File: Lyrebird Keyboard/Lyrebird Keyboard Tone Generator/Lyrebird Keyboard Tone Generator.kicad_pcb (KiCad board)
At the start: 2 copper layers, 8.4 x 51.3 mm, 269 parts, among them IC1 LM358DT, IC10 LM358DT, IC11 LM358DT, IC12 LM358DT, IC13 HEF4069UBT,653, IC14 HEF4069UBT,653, IC15 MC14024BDG, IC16 MC14024BDG, IC17 MC14024BDG, IC18 MC14024BDG, IC19 MC14024BDG, IC2 LM358DT, IC20 MC14024BDG, IC21 MC14024BDG, IC22 MC14024BDG, IC23 MC14024BDG, IC24 MC14024BDG, IC25 MC14024BDG, IC26 MC14024BDG, IC3 LM358DT, IC4 LM358DT, IC5 LM358DT, IC6 LM358DT, IC7 LM358DT, IC8 LM358DT, IC9 LM358DT, J1 Edge Connector, J10 C# 4434 Hz, J11 G# 6642 Hz, J12 D 4697 Hz, J13 F# 5923 Hz, J2 A 3520 Hz, J3 D# 4976 Hz, J4 A# 3726 Hz, J5 E 5274 Hz, J6 B 3949 Hz, J7 F 5590 Hz, J8 C 4188 Hz, J9 G 6275 Hz

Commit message: Further Tone Generator Work, Diode mixers placed
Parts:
- C1, C10, C11, C12, C7, C8, C9, IC1, IC10, IC11, IC12, IC7, IC8, IC9, J11, J13, J2, J3, J5, J7, J9, R1, R2, R25, R26, R27, R28, R29, R3, R30, R31, R32, R33, R34, R35, R36, R37, R38, R39, R4, R40, R41, R42, R43, R44, R45, R46, R47, R48, Z1, Z13, Z14, Z15, Z16, Z17, Z18, Z19, Z2, Z20, Z21, Z22, Z23, Z24: moved to F.Cu
- D1, D10, D100, D101, D102, D103, D104, D105, D106, D107, D108, D109, D11, D110, D111, D112, D113, D114, D115, D116, D117, D118, D119, D12, D120, D121, D122, D123, D124, D125, D126, D127, D128, D129, D130, D131, D132, D133, D134, D135, D136, D137, D138, D139, D14, D140, D141, D142, D143, D144, D145, D146, D15, D16, D17, D18, D19, D2, D20, D21, D22, D23, D24, D25, D26, D27, D28, D29, D3, D30, D31, D32, D33, D34, D35, D36, D37, D38, D39, D4, D40, D41, D42, D43, D44, D45, D46, D47, D48, D49, D5, D50, D51, D52, D53, D54, D55, D56, D57, D58, D59, D6, D60, D61, D62, D63, D64, D65, D66, D67, D68, D69, D7, D70, D71, D72, D73, D74, D75, D76, D77, D78, D79, D8, D80, D81, D82, D83, D84, D85, D86, D87, D88, D89, D9, D90, D91, D92, D93, D94, D95, D96, D97, D98, D99: value 1N4148W -> 1N4148; footprint Diode_SMD:D_SOD-123 -> Diode_THT:D_DO-35_SOD27_P7.62mm_Horizontal
- IC15, IC16, IC17, IC18, IC19, IC20, IC21, IC22, IC23, IC24, IC25, IC26: value MC14024BDG -> CD4024BE; footprint SamacSys_Parts:SOIC127P600X175-14N -> SamacSys_Parts:DIP794W53P254L1930H508Q14N
- moved IC13 244.6 mm to (256.8, 83.6)
- moved IC14 216.1 mm to (237.2, 95.8)
- moved C1 144.7 mm to (216.0, 153.3), turned to 0 degrees
- moved IC1 144.7 mm to (216.0, 153.3), turned to 0 degrees
- moved J2 144.7 mm to (216.0, 153.3), turned to 0 degrees
- moved R1 144.7 mm to (216.0, 153.3), turned to 0 degrees
- moved R2 144.7 mm to (216.0, 153.3), turned to 0 degrees
- moved R3 144.7 mm to (216.0, 153.3), turned to 0 degrees
- moved R4 144.7 mm to (216.0, 153.3), turned to 0 degrees
- moved Z1 144.7 mm to (216.0, 153.3), turned to 0 degrees
- moved Z2 144.7 mm to (216.0, 153.3), turned to 0 degrees
- moved J9 131.7 mm to (215.3, 65.7)
- moved Z22 131.4 mm to (220.4, 71.5), turned to 0 degrees
- moved Z16 128.0 mm to (215.8, 71.5), turned to 0 degrees
- moved J4 126.3 mm to (186.9, 65.8), turned to 180 degrees
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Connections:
- D10 pad 1: Q5 -> Q5A
- D100 pad 1: Q2 -> Q3F#
- D100 pad 2: F#50S -> F#38S
- D101 pad 1: Q2 -> Q3G
- D101 pad 2: G51S -> G39S
- D102 pad 1: Q2 -> Q3G#
- D102 pad 2: G#52S -> G#40S
- D103 pad 1: Q3 -> Q3D#
- D104 pad 1: Q3 -> Q3E
- D105 pad 1: Q3 -> Q3F
- D106 pad 1: Q3 -> Q4F#
- D106 pad 2: F#50S -> F#38S
- D107 pad 1: Q3 -> Q4G
- D107 pad 2: G51S -> G39S
- D108 pad 1: Q3 -> Q4G#
- D108 pad 2: G#52S -> G#40S
- D109 pad 1: Q3 -> Q3D#
- D11 pad 1: Q5 -> Q5A
- D110 pad 1: Q3 -> Q3E
- D111 pad 1: Q3 -> Q3F
- D112 pad 1: Q3 -> Q4F#
- D112 pad 2: F#38S -> F#26S
- D113 pad 1: Q3 -> Q4G
- D113 pad 2: G39S -> G27S
- D114 pad 1: Q3 -> Q4G#
- D114 pad 2: G#40S -> G#28S
- D115 pad 1: Q4 -> Q4D#
- D116 pad 1: Q4 -> Q4E
- D117 pad 1: Q4 -> Q4F
- D118 pad 1: Q4 -> Q5F#
- D118 pad 2: F#38S -> F#26S
- D119 pad 1: Q4 -> Q5G
- D119 pad 2: G39S -> G27S
- D12 pad 1: Q6 -> Q6A
- D120 pad 1: Q4 -> Q5G#
- D120 pad 2: G#40S -> G#28S
- D121 pad 1: Q4 -> Q4D#
- D122 pad 1: Q4 -> Q4E
- D123 pad 1: Q4 -> Q4F
- D124 pad 1: Q4 -> Q5F#
- D124 pad 2: F#26S -> F#14S
- D125 pad 1: Q4 -> Q5G
- D125 pad 2: G27S -> G15S
- D126 pad 1: Q4 -> Q5G#
- D126 pad 2: G#28S -> G#16S
- D127 pad 1: Q5 -> Q5D#
- D128 pad 1: Q5 -> Q5E
- D129 pad 1: Q5 -> Q5F
- D130 pad 1: Q5 -> Q6F#
- D130 pad 2: F#26S -> F#14S
- D131 pad 1: Q5 -> Q6G
- D131 pad 2: G27S -> G15S
- D132 pad 1: Q5 -> Q6G#
- D132 pad 2: G#28S -> G#16S
- D133 pad 1: Q5 -> Q5D#
- D134 pad 1: Q5 -> Q5E
- D135 pad 1: Q5 -> Q5F
- D136 pad 1: Q5 -> Q6F#
- D136 pad 2: F#14S -> F#2S
- D137 pad 1: Q5 -> Q6G
- D137 pad 2: G15S -> G3S
- D138 pad 1: Q5 -> Q6G#
- D138 pad 2: G#16S -> G#4S
- D139 pad 1: Q6 -> Q6D#
- D14 pad 1: Q1 -> Q1A#
- D140 pad 1: Q6 -> Q6E
- D141 pad 1: Q6 -> Q6F
- D142 pad 1: Q6 -> Q7F#
- D142 pad 2: F#14S -> F#2S
- D143 pad 1: Q6 -> Q7G
- D143 pad 2: G15S -> G3S
- D144 pad 1: Q6 -> Q7G#
- D144 pad 2: G#16S -> G#4S
- D145 pad 1: Q6 -> Q6F
- D146 pad 1: Q7 -> Q7F
- D15 pad 1: Q1 -> Q1A#
- D16 pad 1: Q2 -> Q2A#
- D17 pad 1: Q2 -> Q2A#
- D18 pad 1: Q3 -> Q3A#
- D19 pad 1: Q3 -> Q3A#
- D2 pad 1: Q1 -> Q1A
- D20 pad 1: Q4 -> Q4A#
- D21 pad 1: Q4 -> Q4A#
- D22 pad 1: Q5 -> Q5A#
- D23 pad 1: Q5 -> Q5A#
- D24 pad 1: Q6 -> Q6A#
- D26 pad 1: Q1 -> Q1B
- D27 pad 1: Q1 -> Q1B
- D28 pad 1: Q2 -> Q2B
- D29 pad 1: Q2 -> Q2B
- D3 pad 1: Q1 -> Q1A
- D30 pad 1: Q3 -> Q3B
- D31 pad 1: Q3 -> Q3B
- D32 pad 1: Q4 -> Q4B
- D33 pad 1: Q4 -> Q4B
- D34 pad 1: Q5 -> Q5B
- D35 pad 1: Q5 -> Q5B
- D36 pad 1: Q6 -> Q6B
- D38 pad 1: Q1 -> Q1C
- D39 pad 1: Q1 -> Q1C
- D4 pad 1: Q2 -> Q2A
- D40 pad 1: Q2 -> Q2C
- D41 pad 1: Q2 -> Q2C
- D42 pad 1: Q3 -> Q3C
- D43 pad 1: Q3 -> Q3C
- D44 pad 1: Q4 -> Q4C
- D45 pad 1: Q4 -> Q4C
- D46 pad 1: Q5 -> Q5C
- D47 pad 1: Q5 -> Q5C
- D48 pad 1: Q6 -> Q6C
- D5 pad 1: Q2 -> Q2A
- D50 pad 1: Q1 -> Q1C#
- D51 pad 1: Q1 -> Q1C#
- D52 pad 1: Q2 -> Q2C#
- D53 pad 1: Q2 -> Q2C#
- D54 pad 1: Q3 -> Q3C#
- D55 pad 1: Q3 -> Q3C#
- D56 pad 1: Q4 -> Q4C#
- D57 pad 1: Q4 -> Q4C#
- D58 pad 1: Q5 -> Q5C#
- D59 pad 1: Q5 -> Q5C#
- D6 pad 1: Q3 -> Q3A
- D60 pad 1: Q6 -> Q6C#
- D62 pad 1: Q1 -> Q1D
- D63 pad 1: Q1 -> Q1D
- D64 pad 1: Q2 -> Q2D
- D65 pad 1: Q2 -> Q2D
- D66 pad 1: Q3 -> Q3D
- D67 pad 1: Q3 -> Q3D
- D68 pad 1: Q4 -> Q4D
- D69 pad 1: Q4 -> Q4D
- D7 pad 1: Q3 -> Q3A
- D70 pad 1: Q5 -> Q5D
- D71 pad 1: Q5 -> Q5D
- D72 pad 1: Q6 -> Q6D
- D76 pad 1: Q6 -> Q1F#
- D76 pad 2: F#2S -> F#62S
- D77 pad 1: Q6 -> Q1G
- D77 pad 2: G3S -> G63S
- D78 pad 1: Q7 -> Q2G
- D78 pad 2: G3S -> G63S
- D79 pad 1: Q1 -> Q1D#
- D8 pad 1: Q4 -> Q4A
- D80 pad 1: Q1 -> Q1E
- D81 pad 1: Q1 -> Q1F
- D82 pad 1: Q7 -> Q2F#
- D82 pad 2: F#2S -> F#62S
- D83 pad 1: Q6 -> Q1G#
- D83 pad 2: G#4S -> G#64S
- D84 pad 1: Q7 -> Q2G#
- D84 pad 2: G#4S -> G#64S
- D85 pad 1: Q1 -> Q1D#
- D86 pad 1: Q1 -> Q1E
- D87 pad 1: Q1 -> Q1F
- D88 pad 1: Q1 -> Q2F#
- D88 pad 2: F#62S -> F#50S
- D89 pad 1: Q1 -> Q2G
- D89 pad 2: G63S -> G51S
- D9 pad 1: Q4 -> Q4A
- D90 pad 1: Q1 -> Q2G#
- D90 pad 2: G#64S -> G#52S
- D91 pad 1: Q2 -> Q2D#
- D92 pad 1: Q2 -> Q2E
- D93 pad 1: Q2 -> Q2F
- D94 pad 1: Q2 -> Q3F#
- D94 pad 2: F#62S -> F#50S
- D95 pad 1: Q2 -> Q3G
- D95 pad 2: G63S -> G51S
- D96 pad 1: Q2 -> Q3G#
- D96 pad 2: G#64S -> G#52S
- D97 pad 1: Q2 -> Q2D#
- D98 pad 1: Q2 -> Q2E
- D99 pad 1: Q2 -> Q2F
- IC15 pad 11: Q2 -> Q2A
- IC15 pad 12: Q1 -> Q1A
- IC15 pad 4: Q6 -> Q6A
- IC15 pad 5: Q5 -> Q5A
- IC15 pad 6: Q4 -> Q4A
- IC15 pad 9: Q3 -> Q3A
- IC16 pad 11: Q2 -> Q2A#
- IC16 pad 12: Q1 -> Q1A#
- IC16 pad 4: Q6 -> Q6A#
- IC16 pad 5: Q5 -> Q5A#
- IC16 pad 6: Q4 -> Q4A#
- IC16 pad 9: Q3 -> Q3A#
- IC17 pad 11: Q2 -> Q2B
- IC17 pad 12: Q1 -> Q1B
- IC17 pad 4: Q6 -> Q6B
- IC17 pad 5: Q5 -> Q5B
- IC17 pad 6: Q4 -> Q4B
- IC17 pad 9: Q3 -> Q3B
- IC18 pad 11: Q2 -> Q2C
- IC18 pad 12: Q1 -> Q1C
- IC18 pad 4: Q6 -> Q6C
- IC18 pad 5: Q5 -> Q5C
- IC18 pad 6: Q4 -> Q4C
- IC18 pad 9: Q3 -> Q3C
- IC19 pad 11: Q2 -> Q2C#
- IC19 pad 12: Q1 -> Q1C#
- IC19 pad 4: Q6 -> Q6C#
- IC19 pad 5: Q5 -> Q5C#
- IC19 pad 6: Q4 -> Q4C#
- IC19 pad 9: Q3 -> Q3C#
- IC20 pad 11: Q2 -> Q2D
- IC20 pad 12: Q1 -> Q1D
- IC20 pad 4: Q6 -> Q6D
- IC20 pad 5: Q5 -> Q5D
- IC20 pad 6: Q4 -> Q4D
- IC20 pad 9: Q3 -> Q3D
- IC21 pad 11: Q2 -> Q2D#
- IC21 pad 12: Q1 -> Q1D#
- IC21 pad 4: Q6 -> Q6D#
- IC21 pad 5: Q5 -> Q5D#
- IC21 pad 6: Q4 -> Q4D#
- IC21 pad 9: Q3 -> Q3D#
- IC22 pad 11: Q2 -> Q2E
- IC22 pad 12: Q1 -> Q1E
- IC22 pad 4: Q6 -> Q6E
- IC22 pad 5: Q5 -> Q5E
- IC22 pad 6: Q4 -> Q4E
- IC22 pad 9: Q3 -> Q3E
- IC23 pad 11: Q2 -> Q2F
- IC23 pad 12: Q1 -> Q1F
- IC23 pad 3: Q7 -> Q7F
- IC23 pad 4: Q6 -> Q6F
- IC23 pad 5: Q5 -> Q5F
- IC23 pad 6: Q4 -> Q4F
- IC23 pad 9: Q3 -> Q3F
- IC24 pad 11: Q2 -> Q2F#
- IC24 pad 12: Q1 -> Q1F#
- IC24 pad 3: unconnected-(IC24-Q7-Pad3) -> Q7F#
- IC24 pad 4: Q6 -> Q6F#
- IC24 pad 5: Q5 -> Q5F#
- IC24 pad 6: Q4 -> Q4F#
- IC24 pad 9: Q3 -> Q3F#
- IC25 pad 11: Q2 -> Q2G
- IC25 pad 12: Q1 -> Q1G
- IC25 pad 3: Q7 -> Q7G
- IC25 pad 4: Q6 -> Q6G
- IC25 pad 5: Q5 -> Q5G
- IC25 pad 6: Q4 -> Q4G
- IC25 pad 9: Q3 -> Q3G
- IC26 pad 11: Q2 -> Q2G#
- IC26 pad 12: Q1 -> Q1G#
- IC26 pad 3: Q7 -> Q7G#
- IC26 pad 4: Q6 -> Q6G#
- IC26 pad 5: Q5 -> Q5G#
- IC26 pad 6: Q4 -> Q4G#
- IC26 pad 9: Q3 -> Q3G#
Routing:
- net +15V: track 0.00 -> 405.4 mm
- net -15V: track 0.00 -> 183.7 mm
- net E36S: track 0.00 -> 157.0 mm
- net G39S: track 0.00 -> 153.7 mm
- net D#35S: track 0.00 -> 150.3 mm
- net F37S: track 0.00 -> 149.0 mm
- net F#38S: track 0.00 -> 140.2 mm
- net D#23S: track 0.00 -> 138.4 mm
- net F25S: track 0.00 -> 138.4 mm
- net E24S: track 0.00 -> 135.6 mm
- net D#11S: track 0.00 -> 133.5 mm
- net F13S: track 0.00 -> 132.8 mm
- net E12S: track 0.00 -> 130.6 mm
- net F1S: track 0.00 -> 127.7 mm
- net D#47S: track 0.00 -> 127.3 mm
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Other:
- board size 8.4 x 51.3 mm -> 186.8 x 75.5 mm
- copper layers 2 -> 4

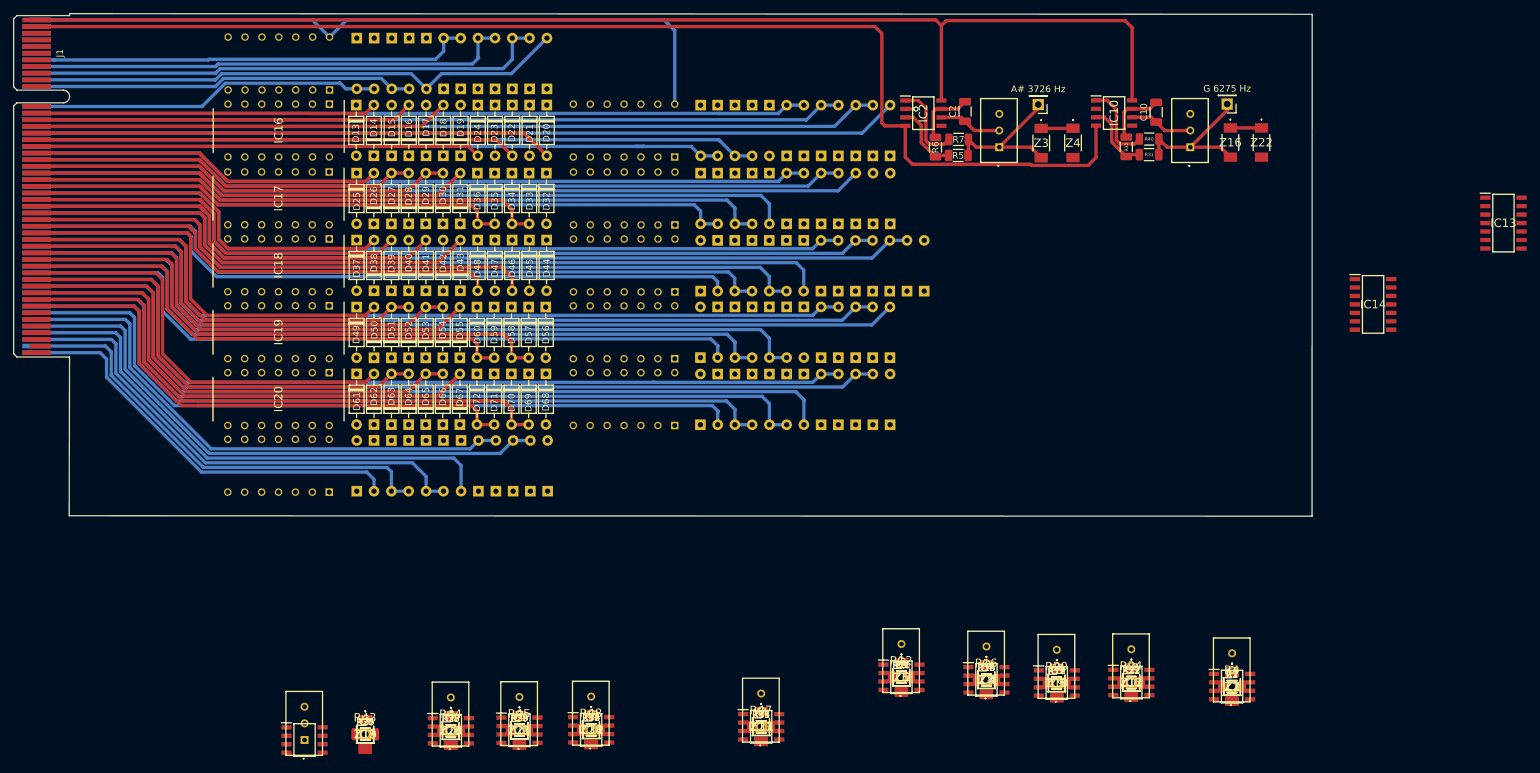
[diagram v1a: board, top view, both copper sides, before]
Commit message: Major Design Changes
Completed Tone Generator Board, board now only provides base notes, individual notes will be generated on the wave shaping boards.

Made major changes to pci slot config, and have increased grounding of the slots.

May need decoupling capacitors on tone generator board, but tight for room
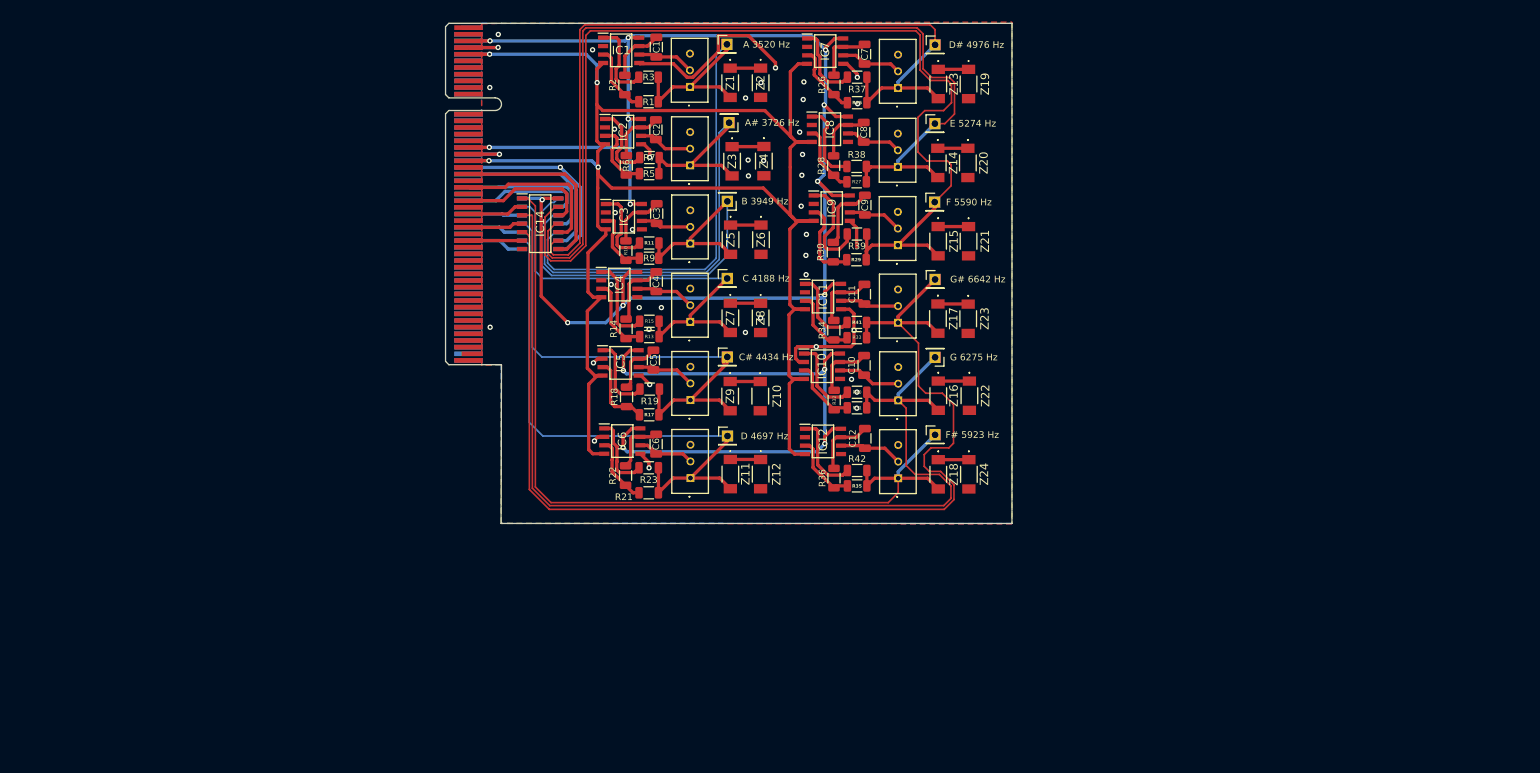
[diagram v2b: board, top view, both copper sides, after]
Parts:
- removed D1, D10, D100, D101, D102, D103, D104, D105, D106, D107, D108, D109, D11, D110, D111, D112, D113, D114, D115, D116, D117, D118, D119, D12, D120, D121, D122, D123, D124, D125, D126, D127, D128, D129, D13, D130, D131, D132, D133, D134, D135, D136, D137, D138, D139, D14, D140, D141, D142, D143, D144, D145, D146, D15, D16, D17, D18, D19, D2, D20, D21, D22, D23, D24, D25, D26, D27, D28, D29, D3, D30, D31, D32, D33, D34, D35, D36, D37, D38, D39, D4, D40, D41, D42, D43, D44, D45, D46, D47, D48, D49, D5, D50, D51, D52, D53, D54, D55, D56, D57, D58, D59, D6, D60, D61, D62, D63, D64, D65, D66, D67, D68, D69, D7, D70, D71, D72, D73, D74, D75, D76, D77, D78, D79, D8, D80, D81, D82, D83, D84, D85, D86, D87, D88, D89, D9, D90, D91, D92, D93, D94, D95, D96, D97, D98, D99: 1N4148, Diode_THT:D_DO-35_SOD27_P7.62mm_Horizontal
- removed IC15, IC16, IC17, IC18, IC19, IC20, IC21, IC22, IC23, IC24, IC25, IC26: CD4024BE, SamacSys_Parts:DIP794W53P254L1930H508Q14N
- IC13: moved to B.Cu
- moved IC13 144.7 mm to (112.1, 83.7), turned to 180 degrees
- moved J3 134.4 mm to (171.4, 56.8)
- moved Z19 133.3 mm to (176.4, 62.7)
- moved IC1 132.5 mm to (124.2, 57.7)
- moved R43 132.5 mm to (165.8, 63.3)
- moved Z13 130.2 mm to (171.9, 62.7)
- moved IC7 129.7 mm to (154.9, 57.8)
- moved C1 129.3 mm to (129.5, 57.2), turned to 90 degrees
- moved R2 128.4 mm to (124.8, 62.9), turned to -90 degrees
- moved R3 126.8 mm to (128.3, 61.7), turned to 180 degrees
- moved C7 126.8 mm to (160.8, 58.2), turned to 90 degrees
- moved IC14 125.7 mm to (112.1, 83.7)
- moved R1 124.1 mm to (128.3, 65.4)
- moved R37 123.3 mm to (159.7, 61.7), turned to 180 degrees
- moved J2 122.8 mm to (140.1, 56.8)
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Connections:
- IC13 pad 1: A (3520 Hz) -> B (3949 Hz)
- IC13 pad 10: C# (4434 Hz) INV -> TONE 5
- IC13 pad 12: C (4188 Hz) INV -> TONE 4
- IC13 pad 2: A (3520 Hz) INV -> TONE 3
- IC13 pad 4: A# (3726 Hz) INV -> TONE 2
- IC13 pad 5: B (3949 Hz) -> A (3520 Hz)
- IC13 pad 6: B (3949 Hz) INV -> TONE 1
- IC13 pad 8: D (4697 Hz) INV -> TONE 6
- IC14 pad 1: D# (4976 Hz) -> F# (5923 Hz)
- IC14 pad 10: G (6275 Hz) INV -> TONE 8
- IC14 pad 11: G (6275 Hz) -> E (5274 Hz)
- IC14 pad 12: F# (5923 Hz) INV -> TONE 9
- IC14 pad 13: F# (5923 Hz) -> F (5590 Hz)
- IC14 pad 2: D# (4976 Hz) INV -> TONE 10
- IC14 pad 3: E (5274 Hz) -> G (6275 Hz)
- IC14 pad 4: E (5274 Hz) INV -> TONE 11
- IC14 pad 5: F (5590 Hz) -> G# (6642 Hz)
- IC14 pad 6: F (5590 Hz) INV -> TONE 12
- IC14 pad 8: G# (6642 Hz) INV -> TONE 7
- IC14 pad 9: G# (6642 Hz) -> D# (4976 Hz)
- J1 pad A1: +15V -> unconnected-(J1-PadA1)
- J1 pad A10: G#40S -> GND
- J1 pad A11: G#52S -> unconnected-(J1-PadA11)
- J1 pad A12: G#64S -> GND
- J1 pad A13: G3S -> unconnected-(J1-PadA13)
- J1 pad A14: G15S -> GND
- J1 pad A15: G27S -> unconnected-(J1-PadA15)
- J1 pad A16: G39S -> GND
- J1 pad A17: G51S -> +15V
- J1 pad A18: G63S -> GND
- J1 pad A19: F#2S -> -15V
- J1 pad A2: -15V -> GND
- J1 pad A20: F#14S -> GND
- J1 pad A21: F#26S -> TONE 1
- J1 pad A22: F#38S -> unconnected-(J1-PadA22)
- J1 pad A23: F#50S -> TONE 2
- J1 pad A24: F#62S -> unconnected-(J1-PadA24)
- J1 pad A25: F1S -> TONE 3
- J1 pad A26: F13S -> unconnected-(J1-PadA26)
- J1 pad A27: F25S -> TONE 4
- J1 pad A28: F37S -> unconnected-(J1-PadA28)
- J1 pad A29: F49S -> TONE 5
- J1 pad A3: GND -> +15V
- J1 pad A30: F61S -> unconnected-(J1-PadA30)
- J1 pad A31: F73S -> TONE 6
- J1 pad A32: E12S -> GND
- J1 pad A33: E24S -> unconnected-(J1-PadA33)
- J1 pad A34: E36S -> GND
- J1 pad A35: E48S -> unconnected-(J1-PadA35)
- J1 pad A36: E60S -> GND
- J1 pad A37: E72S -> unconnected-(J1-PadA37)
- J1 pad A38: D#11S -> GND
- J1 pad A39: D#23S -> unconnected-(J1-PadA39)
- J1 pad A40: D#35S -> GND
- J1 pad A41: D#47S -> unconnected-(J1-PadA41)
- J1 pad A42: D#59S -> GND
- J1 pad A43: D#71S -> unconnected-(J1-PadA43)
- J1 pad A44: A5S -> GND
- J1 pad A45: A17S -> unconnected-(J1-PadA45)
- J1 pad A46: A29S -> GND
- J1 pad A47: A41S -> unconnected-(J1-PadA47)
- J1 pad A48: A53S -> GND
- J1 pad A49: A65S -> unconnected-(J1-PadA49)
- J1 pad A5: GND -> -15V
- J1 pad A6: +VT -> GND
- J1 pad A7: G#4S -> unconnected-(J1-PadA7)
- J1 pad A8: G#16S -> GND
- J1 pad A9: G#28S -> unconnected-(J1-PadA9)
- J1 pad B1: +15V -> unconnected-(J1-PadB1)
- J1 pad B10: EXP8 -> GND
- J1 pad B11: EXP9 -> unconnected-(J1-PadB11)
- J1 pad B12: EXP10 -> GND
- J1 pad B13: A#66S -> unconnected-(J1-PadB13)
- J1 pad B14: A#54S -> GND
- J1 pad B15: A#42S -> unconnected-(J1-PadB15)
- J1 pad B16: A#30S -> GND
- J1 pad B17: A#18S -> +15V
- J1 pad B18: A#6S -> GND
- J1 pad B19: B67S -> -15V
- J1 pad B2: -15V -> GND
- J1 pad B20: B55S -> GND
- J1 pad B21: B43S -> TONE 7
- J1 pad B22: B31S -> unconnected-(J1-PadB22)
- J1 pad B23: B19S -> TONE 8
- J1 pad B24: B7S -> unconnected-(J1-PadB24)
- J1 pad B25: C68S -> TONE 9
- J1 pad B26: C56S -> unconnected-(J1-PadB26)
- J1 pad B27: C44S -> TONE 10
- J1 pad B28: C32S -> unconnected-(J1-PadB28)
- J1 pad B29: C20S -> TONE 11
- J1 pad B3: GND -> +15V
- J1 pad B30: C8S -> unconnected-(J1-PadB30)
- J1 pad B31: C#69S -> TONE 12
- J1 pad B32: C#57S -> GND
- J1 pad B33: C#45S -> unconnected-(J1-PadB33)
- J1 pad B34: C#33S -> GND
- J1 pad B35: C#21S -> unconnected-(J1-PadB35)
- J1 pad B36: C#9S -> GND
- J1 pad B37: D70S -> unconnected-(J1-PadB37)
- J1 pad B38: D58S -> GND
- J1 pad B39: D46S -> unconnected-(J1-PadB39)
- J1 pad B40: D34S -> GND
- J1 pad B41: D22S -> unconnected-(J1-PadB41)
- J1 pad B42: D10S -> GND
- J1 pad B43: EXP1 -> unconnected-(J1-PadB43)
- J1 pad B44: EXP2 -> GND
- J1 pad B45: EXP3 -> unconnected-(J1-PadB45)
- J1 pad B46: EXP4 -> GND
- J1 pad B47: EXP5 -> unconnected-(J1-PadB47)
- J1 pad B48: EXP6 -> GND
- J1 pad B49: EXP7 -> unconnected-(J1-PadB49)
- J1 pad B5: GND -> -15V
- J1 pad B6: +VED -> GND
- J1 pad B7: SUSTAIN -> unconnected-(J1-PadB7)
- J1 pad B8: SOFT -> GND
- J1 pad B9: LINE OUT -> unconnected-(J1-PadB9)
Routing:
- net G# (6642 Hz): track 0.00 -> 165.2 mm
- net F (5590 Hz): track 0.00 -> 161.1 mm
- net E36S: track 157.0 -> 0.00 mm
- net G39S: track 153.7 -> 0.00 mm
- net D#35S: track 150.3 -> 0.00 mm
- net F37S: track 149.0 -> 0.00 mm
- net F#38S: track 140.2 -> 0.00 mm
- net D#23S: track 138.4 -> 0.00 mm
- net F25S: track 138.4 -> 0.00 mm
- net E (5274 Hz): track 0.00 -> 136.7 mm
- net E24S: track 135.6 -> 0.00 mm
- net D#11S: track 133.5 -> 0.00 mm
- net F13S: track 132.8 -> 0.00 mm
- net E12S: track 130.6 -> 0.00 mm
- net F1S: track 127.7 -> 0.00 mm
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- added copper zone on B.Cu, net GND
- added copper zone on F.Cu, net GND
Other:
- board size 186.8 x 75.5 mm -> 76.8 x 75.2 mm
- copper layers 4 -> 2
